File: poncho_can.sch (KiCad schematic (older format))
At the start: 37 parts, among them J10 GS2, J101 DB9_Male_MountingHoles, J102 DB9_Male_MountingHoles, J103 GS2, J104 GS2, J105 GS2, J106 GS2, J7 GS2, J8 GS2, J9 GS2, U101 TJA1051T, U102 TJA1051T

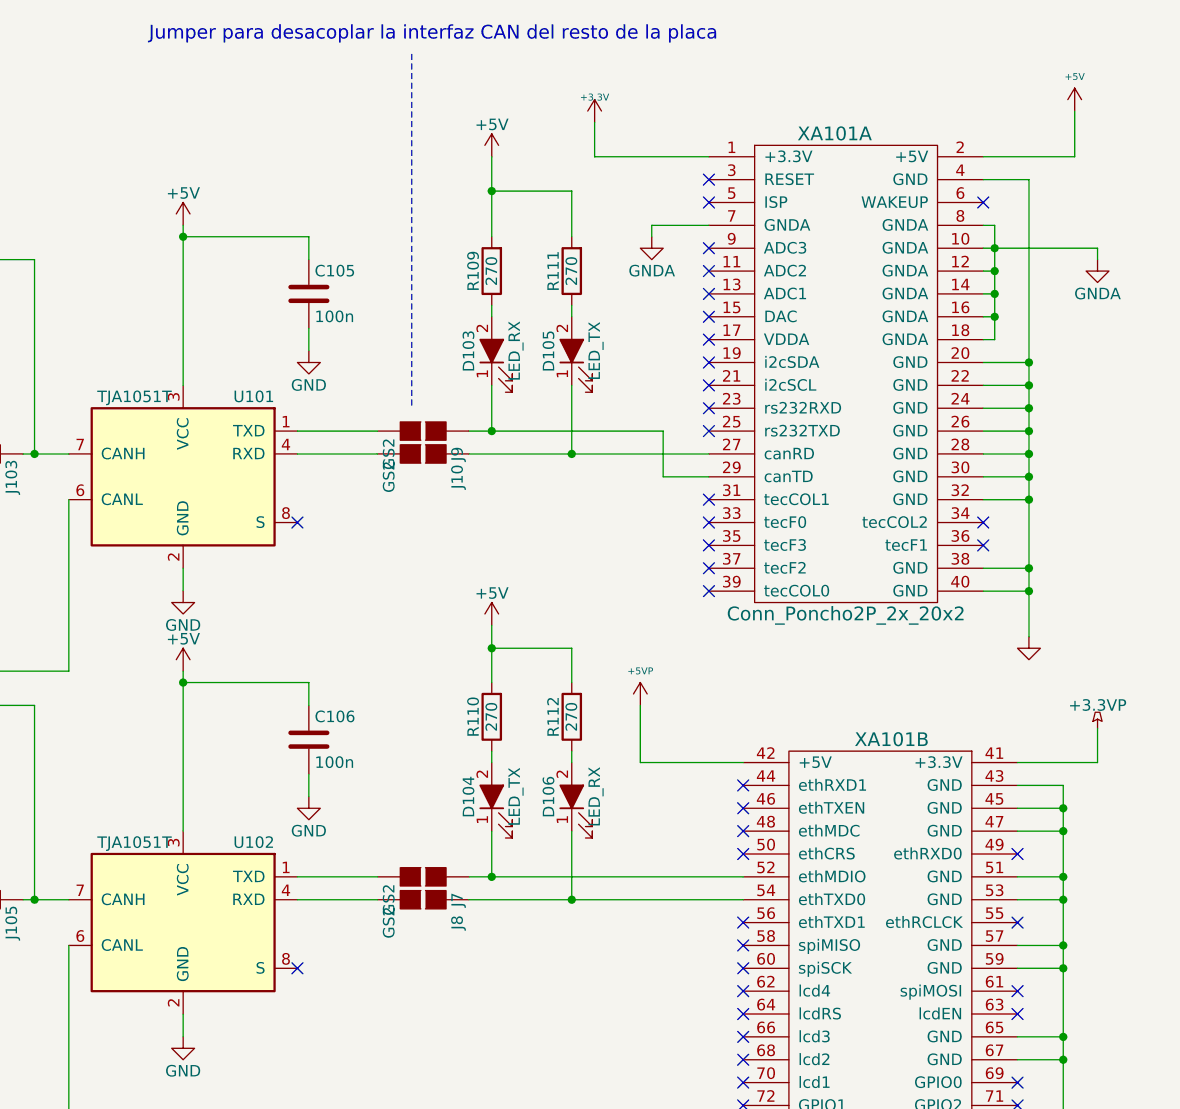
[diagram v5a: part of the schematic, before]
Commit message: Muevo los leds del otro lado de los jumpers de goteo
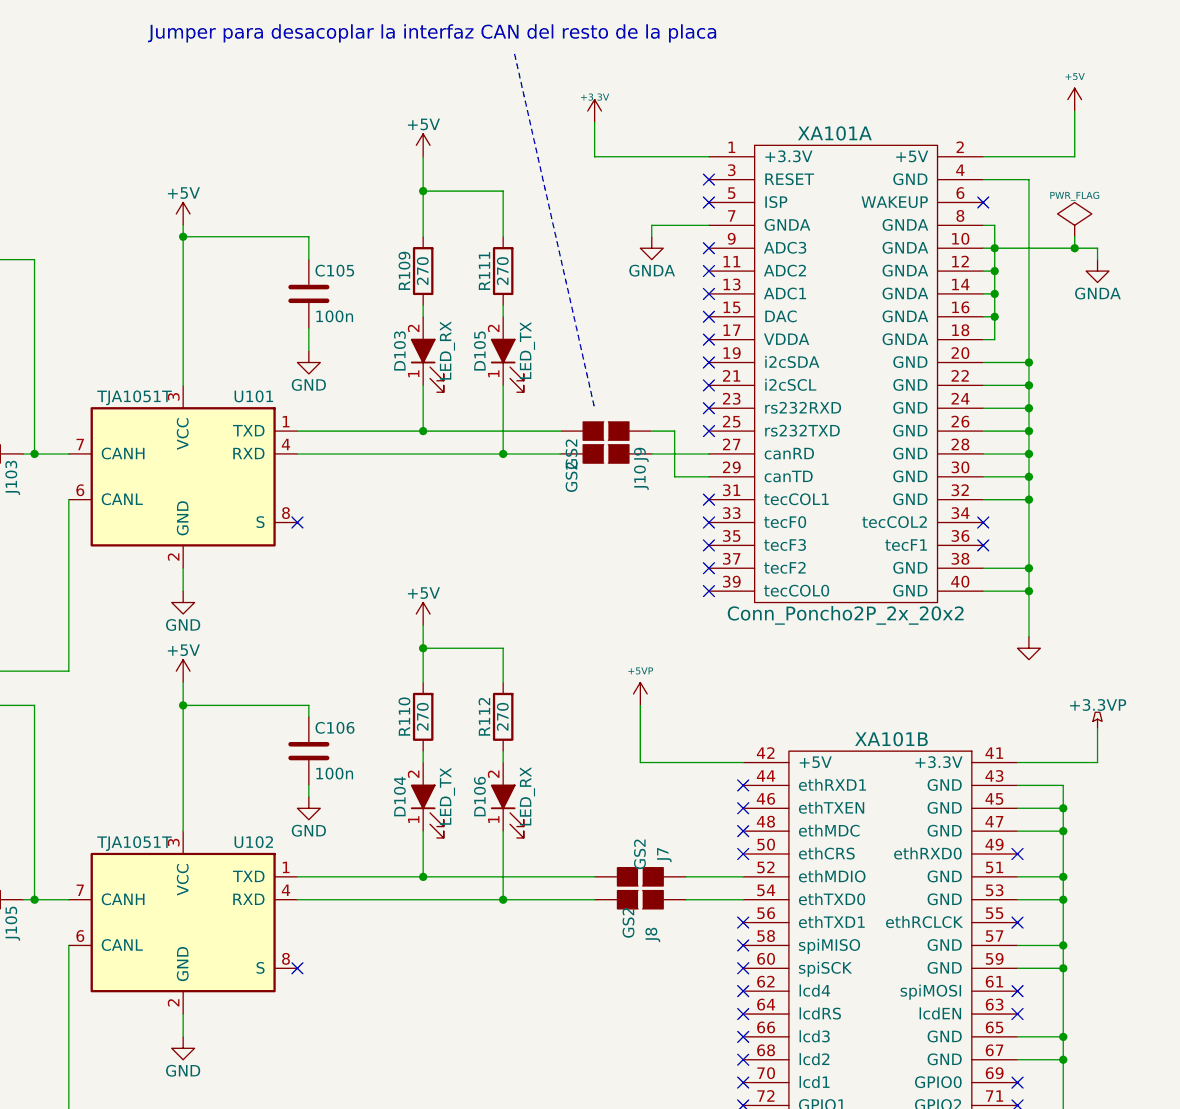
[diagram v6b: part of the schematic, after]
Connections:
- net at J10.1 (G1), XA101.27 (canRD): no longer D105.1 (K)
- net at J9.1 (G1), XA101.29 (canTD): no longer D103.1 (K)
- net at J7.1 (G1), XA101.52 (ethMDIO): no longer D104.1 (K)
- net at J8.1 (G1), XA101.54 (ethTXD0): no longer D106.1 (K)
- net at J10.2 (G2), U101.4 (RXD): now also D105.1 (K)
- net at J9.2 (G2), U101.1 (TXD): now also D103.1 (K)
- net at J8.2 (G2), U102.4 (RXD): now also D106.1 (K)
- net at J7.2 (G2), U102.1 (TXD): now also D104.1 (K)
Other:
- moved on the sheet: C106, D103, D104, D105, D106, J10, J7, J8, J9, R109, R110, R111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

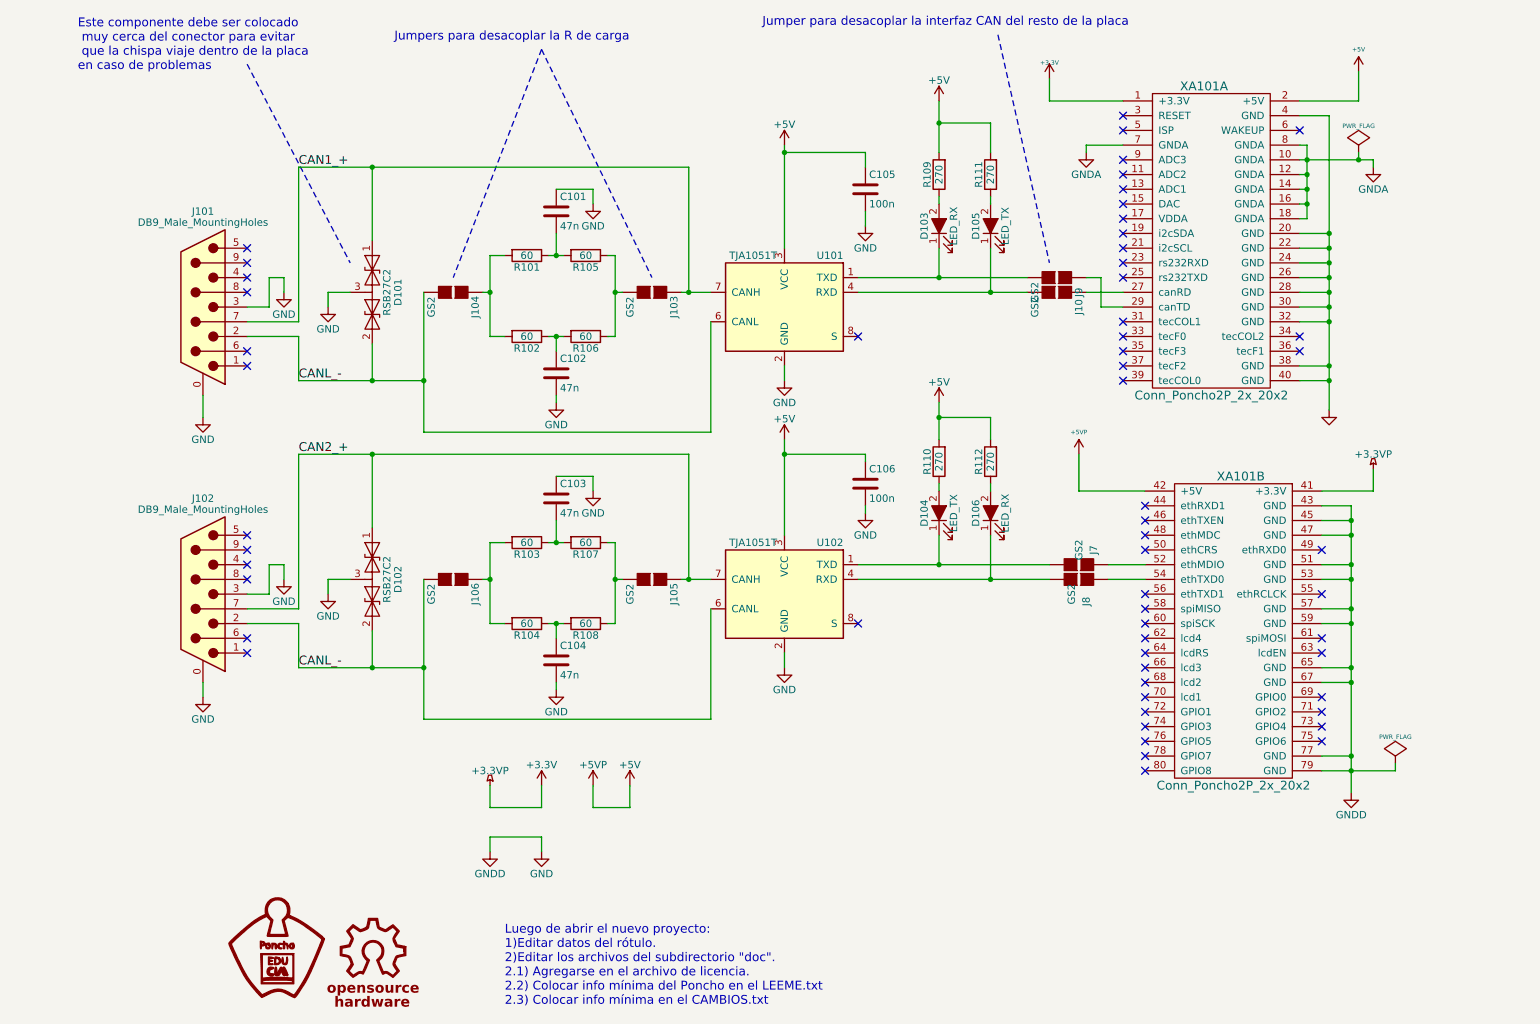
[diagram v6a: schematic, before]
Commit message: Ruteo de los componentes
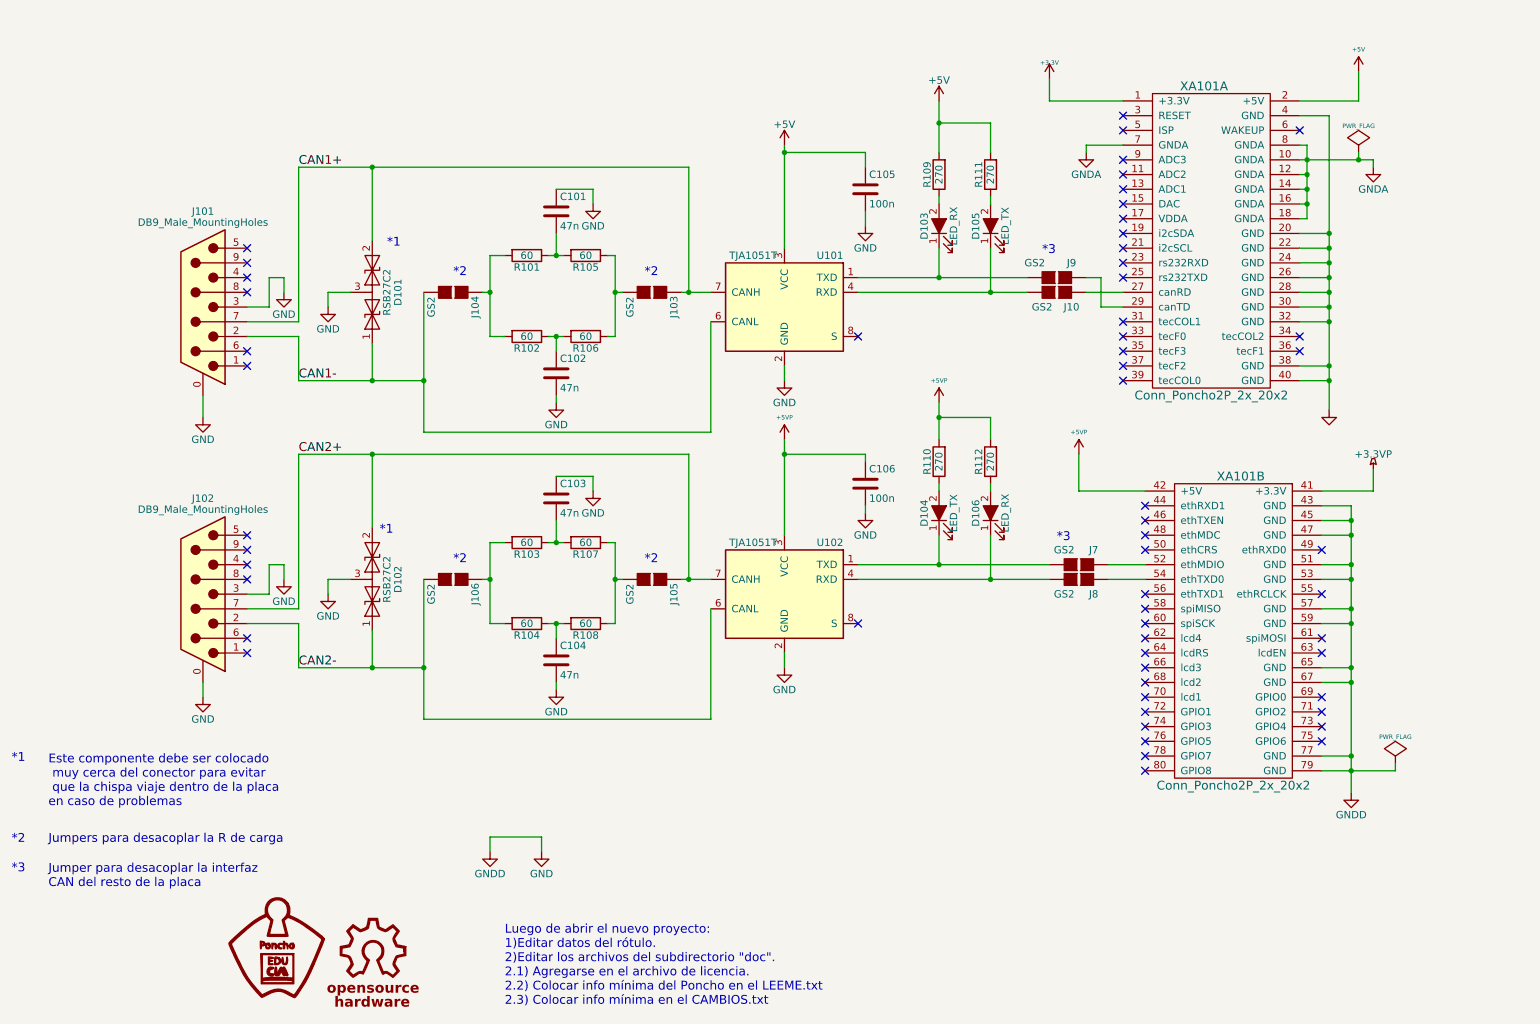
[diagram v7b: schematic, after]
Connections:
- net +3.3VP: no longer XA101.1 (+3.3V)
- net +5V: no longer C106.1, R110.2, R112.2, U102.3 (VCC), XA101.42 (+5V)
- net CAN1_+ renamed CAN1+
- net CAN1+: now also D101.2 (A2); no longer D101.1 (A1)
- net CAN2_+ renamed CAN2+
- net CAN2+: now also D102.2 (A2); no longer D102.1 (A1)
- removed net CANL_-: D101.2 (A2), D102.2 (A2), J101.2, J102.2, J104.2 (G2), J106.2 (G2), U101.6 (CANL), U102.6 (CANL)
- new net +3V3: XA101.1 (+3.3V)
- new net +5VP: C106.1, R110.2, R112.2, U102.3 (VCC), XA101.42 (+5V)
- new net CAN1-: D101.1 (A1), J101.2, J104.2 (G2), U101.6 (CANL)
- new net CAN2-: D102.1 (A1), J102.2, J106.2 (G2), U102.6 (CANL)
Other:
- note added: "*1"
- note added: "*2"
- note added: "*3"
- note added: "Jumper para desacoplar la interfaz \nCAN del resto de la placa"
- note removed: "Jumper para desacoplar la interfaz CAN del resto de la placa"
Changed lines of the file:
@@
 U 1 1 5BA47B7A
 P 7950 2600
-F 0 "J10" H 8050 2750 50  0000 C CNN
-F 1 "GS2" H 8050 2451 50  0000 C CNN
+F 0 "J10" V 8050 2700 50  0000 C CNN
+F 1 "GS2" V 8050 2500 50  0000 C CNN
 F 2 "Connect:GS2" V 8024 2600 50  0001 C CNN
 F 3 "" H 7950 2600 50  0001 C CNN
@@
 U 1 1 5BA47CA2
 P 7950 2500
-F 0 "J9" H 8050 2650 50  0000 C CNN
-F 1 "GS2" H 8050 2351 50  0000 C CNN
+F 0 "J9" V 7850 2600 50  0000 C CNN
+F 1 "GS2" V 7850 2350 50  0000 C CNN
 F 2 "Connect:GS2" V 8024 2500 50  0001 C CNN
 F 3 "" H 7950 2500 50  0001 C CNN
@@
 U 1 1 5BA48FB9
 P 8100 4550
-F 0 "J8" H 8250 4600 50  0000 C CNN
-F 1 "GS2" H 8200 4500 50  0000 C CNN
+F 0 "J8" V 8200 4650 50  0000 C CNN
+F 1 "GS2" V 8200 4450 50  0000 C CNN
 F 2 "Connect:GS2" V 8174 4550 50  0001 C CNN
 F 3 "" H 8100 4550 50  0001 C CNN
@@
 U 1 1 5BA48FBF
 P 8100 4450
-F 0 "J7" H 8000 4550 50  0000 C CNN
-F 1 "GS2" H 8000 4450 50  0000 C CNN
+F 0 "J7" V 8000 4550 50  0000 C CNN
+F 1 "GS2" V 8000 4350 50  0000 C CNN
 F 2 "Connect:GS2" V 8174 4450 50  0001 C CNN
 F 3 "" H 8100 4450 50  0001 C CNN
@@
 F 3 "" H 3150 2600 50  0001 C CNN
 	1    3300 2600
-	0    1    1    0
+	0    1    -1   0
 $EndComp
 $Comp
@@
 $EndComp
 $Comp
-L +5V #PWR018
-U 1 1 5BB59E13
-P 6100 3600
-F 0 "#PWR018" H 6100 3450 50  0001 C CNN
-F 1 "+5V" H 6100 3740 50  0000 C CNN
-F 2 "" H 6100 3600 50  0000 C CNN
-F 3 "" H 6100 3600 50  0000 C CNN
-	1    6100 3600
-	1    0    0    -1
-$EndComp
-$Comp
 L GS2 J106
 U 1 1 5BB59E19
@@
 F 3 "" H 3150 4550 50  0001 C CNN
 	1    3300 4550
-	0    1    1    0
+	0    1    -1   0
 $EndComp
 $Comp
@@
 	1    7500 3750
 	-1   0    0    1
-$EndComp
-$Comp
-L +5V #PWR024
-U 1 1 5BBC57AB
-P 7150 3350
-F 0 "#PWR024" H 7150 3200 50  0001 C CNN
-F 1 "+5V" H 7150 3490 50  0000 C CNN
-F 2 "" H 7150 3350 50  0000 C CNN
-F 3 "" H 7150 3350 50  0000 C CNN
-	1    7150 3350
-	1    0    0    -1
 $EndComp
 $Comp
@@
 $EndComp
 $Comp
-L +3.3VP #PWR028
-U 1 1 5BBC9D66
-P 4100 5950
-F 0 "#PWR028" H 4250 5900 50  0001 C CNN
-F 1 "+3.3VP" H 4100 6050 50  0000 C CNN
-F 2 "" H 4100 5950 50  0000 C CNN
-F 3 "" H 4100 5950 50  0000 C CNN
-	1    4100 5950
-	1    0    0    -1
-$EndComp
-$Comp
-L +3.3V #PWR029
-U 1 1 5BBC9DC6
-P 4450 5950
-F 0 "#PWR029" H 4450 5800 50  0001 C CNN
-F 1 "+3.3V" H 4450 6090 50  0000 C CNN
-F 2 "" H 4450 5950 50  0000 C CNN
-F 3 "" H 4450 5950 50  0000 C CNN
-	1    4450 5950
-	1    0    0    -1
-$EndComp
-$Comp
-L +5VP #PWR030
-U 1 1 5BBC9E26
-P 4800 5950
-F 0 "#PWR030" H 4800 5800 50  0001 C CNN
-F 1 "+5VP" H 4800 6090 50  0000 C CNN
-F 2 "" H 4800 5950 50  0000 C CNN
-F 3 "" H 4800 5950 50  0000 C CNN
-	1    4800 5950
-	1    0    0    -1
-$EndComp
-$Comp
-L +5V #PWR031
-U 1 1 5BBC9E86
-P 5050 5950
-F 0 "#PWR031" H 5050 5800 50  0001 C CNN
-F 1 "+5V" H 5050 6090 50  0000 C CNN
-F 2 "" H 5050 5950 50  0000 C CNN
-F 3 "" H 5050 5950 50  0000 C CNN
-	1    5050 5950
-	1    0    0    -1
-$EndComp
-$Comp
-L GNDD #PWR032
+L GNDD #PWR028
 U 1 1 5BBC9EE6
 P 4100 6400
-F 0 "#PWR032" H 4100 6150 50  0001 C CNN
+F 0 "#PWR028" H 4100 6150 50  0001 C CNN
 F 1 "GNDD" H 4100 6250 50  0000 C CNN
 F 2 "" H 4100 6400 50  0000 C CNN
@@
 $EndComp
 $Comp
-L GND #PWR033
+L GND #PWR029
 U 1 1 5BBC9F46
 P 4450 6400
-F 0 "#PWR033" H 4450 6150 50  0001 C CNN
+F 0 "#PWR029" H 4450 6150 50  0001 C CNN
 F 1 "GND" H 4450 6250 50  0000 C CNN
 F 2 "" H 4450 6400 50  0000 C CNN
@@
 	1    0    0    -1
 $EndComp
-Text Notes 1300 1100 0    60   ~ 0
-Este componente debe ser colocado\n muy cerca del conector para evitar\n que la chispa viaje dentro de la placa \nen caso de problemas
-Text Notes 3450 900  0    60   ~ 0
+Text Notes 1100 6350 0    60   ~ 0
 Jumpers para desacoplar la R de carga
-Text Notes 5950 800  0    60   ~ 0
-Jumper para desacoplar la interfaz CAN del resto de la placa
+Text Notes 1100 6650 0    60   ~ 0
+Jumper para desacoplar la interfaz \nCAN del resto de la placa
 Text Label 2800 3700 0    60   ~ 0
-CAN2_+
+CAN2+
 Text Label 2800 5150 0    60   ~ 0
-CANL_-
+CAN2-
 Text Label 2800 1750 0    60   ~ 0
-CAN1_+
+CAN1+
 Text Label 2800 3200 0    60   ~ 0
-CANL_-
-$Comp
-L PWR_FLAG #FLG034
+CAN1-
+$Comp
+L PWR_FLAG #FLG030
 U 1 1 5BBD225C
 P 10000 1650
-F 0 "#FLG034" H 10000 1745 30  0001 C CNN
+F 0 "#FLG030" H 10000 1745 30  0001 C CNN
 F 1 "PWR_FLAG" H 10000 1830 30  0000 C CNN
 F 2 "" H 10000 1650 60  0000 C CNN
@@
 	4450 6300 4450 6400
 Wire Wire Line
-	4100 5950 4100 6100
-Wire Wire Line
-	4100 6100 4450 6100
-Wire Wire Line
-	4450 6100 4450 5950
-Wire Wire Line
-	4800 5950 4800 6100
-Wire Wire Line
-	4800 6100 5050 6100
-Wire Notes Line
-	2450 1050 3150 2400
-Wire Notes Line
-	4450 950  3850 2500
-Wire Notes Line
-	4450 950  5200 2500
-Wire Wire Line
 	8300 4450 8550 4450
 Wire Wire Line
@@
 	7150 2300 7150 2500
 Connection ~ 7150 2500
-Wire Notes Line
-	7550 850  7900 2400
 Wire Wire Line
 	6650 4050 6650 4100
@@
 	10000 1650 10000 1700
 Connection ~ 10000 1700
-Wire Wire Line
-	5050 6100 5050 5950
+Text Notes 3400 2300 0    60   ~ 0
+*1
+Text Notes 3350 4250 0    60   ~ 0
+*1
+Text Notes 850  5800 0    60   ~ 0
+*1
+Text Notes 3850 4450 0    60   ~ 0
+*2
+Text Notes 5150 4450 0    60   ~ 0
+*2
+Text Notes 3850 2500 0    60   ~ 0
+*2
+Text Notes 5150 2500 0    60   ~ 0
+*2
+Text Notes 1100 6100 0    60   ~ 0
+Este componente debe ser colocado\n muy cerca del conector para evitar\n que la chispa viaje dentro de la placa \nen caso de problemas
+Text Notes 7850 2350 0    60   ~ 0
+*3
+Text Notes 7950 4300 0    60   ~ 0
+*3
+Text Notes 850  6350 0    60   ~ 0
+*2
+Text Notes 850  6550 0    60   ~ 0
+*3
+$Comp
+L +5VP #PWR?
+U 1 1 5BBD8B38
+P 7150 3350
+F 0 "#PWR?" H 7150 3440 20  0001 C CNN
+F 1 "+5VP" H 7150 3500 30  0000 C CNN
+F 2 "" H 7150 3350 60  0000 C CNN
+F 3 "" H 7150 3350 60  0000 C CNN
+	1    7150 3350
+	-1   0    0    -1
+$EndComp
+$Comp
+L +5VP #PWR?
+U 1 1 5BBD8CA5
+P 6100 3600
+F 0 "#PWR?" H 6100 3690 20  0001 C CNN
+F 1 "+5VP" H 6100 3750 30  0000 C CNN
+F 2 "" H 6100 3600 60  0000 C CNN
+F 3 "" H 6100 3600 60  0000 C CNN
+	1    6100 3600
+	-1   0    0    -1
+$EndComp
 $EndSCHEMATC
